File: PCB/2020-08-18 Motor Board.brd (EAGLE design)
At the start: 66 x 88.9 mm, 21 parts

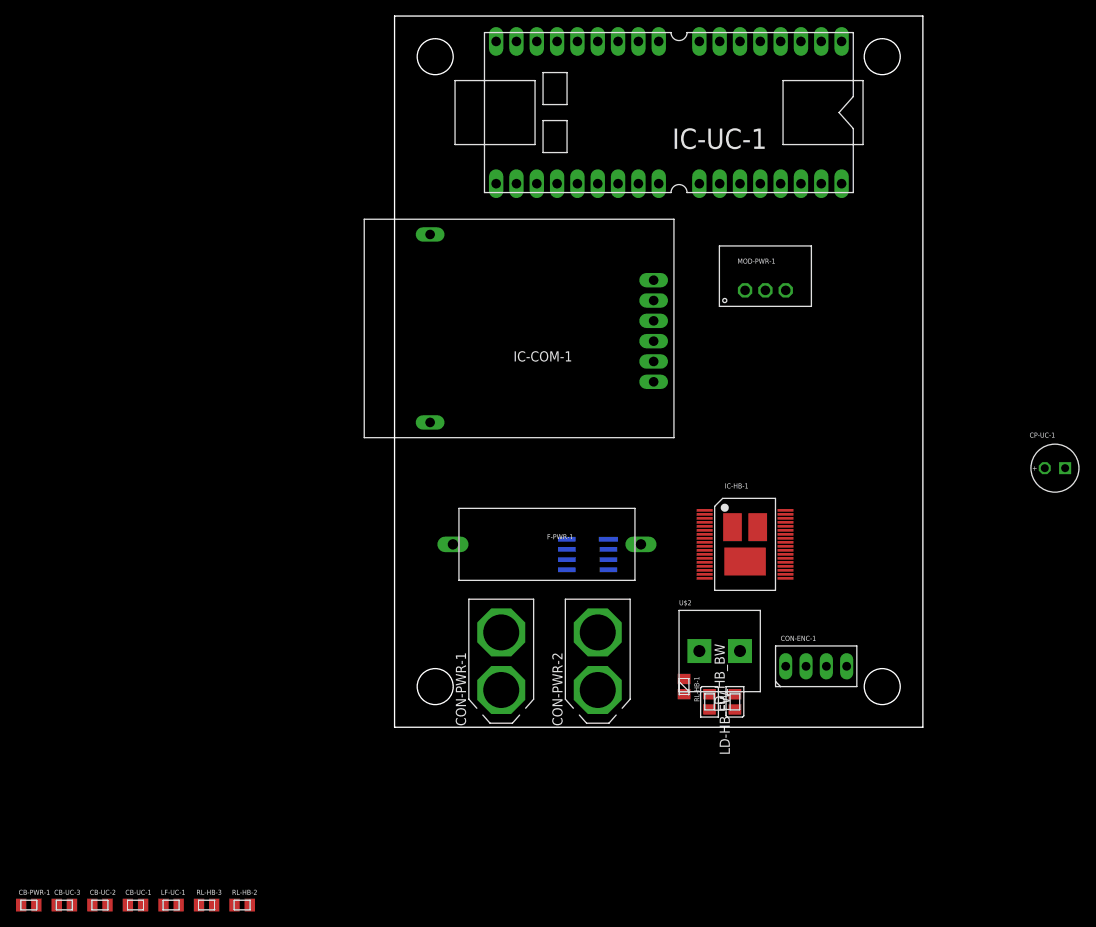
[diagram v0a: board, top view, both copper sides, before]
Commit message: updates schematics, dimensions and placement.
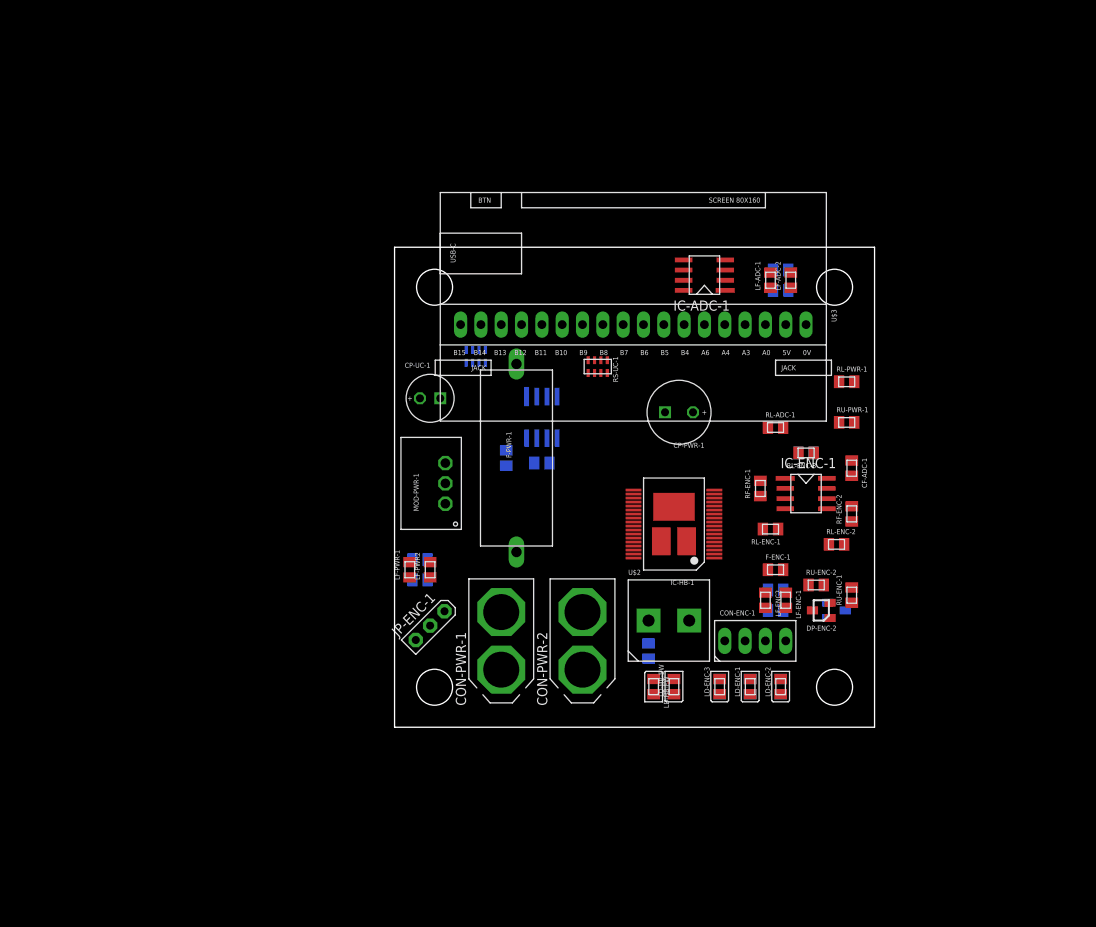
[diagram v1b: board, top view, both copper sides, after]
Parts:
- removed CB-PWR-1, CB-UC-1, CB-UC-2: 100n, Passives:SMD-M2012
- removed CB-UC-3: 10n, Passives:SMD-M2012
- removed IC-COM-1: MODULE-RS485-3MM5-JACK-X2, 2020-08-18 Motor Board:MODULE-RS485-3MM5-JACK-X2
- removed IC-UC-1: LONGAN-NANO, 2020-08-18 Motor Board:LONGAN-NANO
- removed LD_HB_BW: RED, Passives:SMD-M2012-POL
- removed LF-UC-1: BEAD 500mA, Passives:SMD-M2012
- removed RL-HB-2, RL-HB-3: 2.2K, Passives:SMD-M2012
- added CB-ADC-1, CB-ADC-2, CB-ENC-1, CB-ENC-2, CB-PWR-2, CB-PWR-3, CB-PWR1: 100n, Passives:SMD-M2012
- added CF-ADC-1, CF-PWR-1: 10n, Passives:SMD-M2012
- added CP-PWR-1: C+-TH3.5-8.0, Passives:TH-BARREL-3M5-8M0
- added DP-ENC-1, DP-ENC-2: BAT54S-SOT23, 2020-08-18 Motor Board:SOT23
- added F-ENC-1: 500mA, Passives:SMD-M2012
- added IC-ADC-1: MCP6282-SO8, 2020-08-18 Motor Board:SO8
- added IC-ENC-1: LM393-SO8, 2020-08-18 Motor Board:SO8
- added JP-ENC-1: (no value), 2020-08-18 Motor Board:1X03
- added LD-ENC-1, LD-ENC-2, LD-ENC-3: GREEN, Passives:SMD-M2012-POL
- added LD-HB-BW: RED, Passives:SMD-M2012-POL
- added LF-ADC-1, LF-ADC-2, LF-ENC-1, LF-ENC2, LF-PWR-1, LF-PWR2: BEAD 500mA, Passives:SMD-M2012
- added RF-ENC-1, RF-ENC-2, RL-ADC-1, RL-ENC-1, RL-ENC-2, RL-ENC-3, RL-PWR-1, RU-ENC-3, RU-PWR-1: 2.2K, Passives:SMD-M2012
- added RS-ENC-1, RS-ENC-2, RS-ENC-3, RU-ENC-1, RU-ENC-2: 330, Passives:SMD-M2012
- added RS-UC-1, RS-UC-2: RX4-M2012-X4, Passives:SMD-M2012-X4
- added U$3: MODULE-LONGAN-NANO, 2020-08-18 Motor Board:MODULE-LONGAN-NANO
- moved CP-UC-1 78.6 mm to (4.45, 41.1)
- moved MOD-PWR-1 46.7 mm to (6.35, 30.5), turned to 90 degrees
- moved IC-PWR-1 18.1 mm to (18.4, 38.7), turned to 180 degrees
- moved F-PWR-1 11.4 mm to (15.2, 33.7), turned to 90 degrees
- moved IC-HB-1 9.25 mm to (34.9, 25.4), turned to 90 degrees
- moved CON-ENC-1 8.25 mm to (45.1, 10.8)
- moved U$2 7.41 mm to (34.3, 13.3)
- moved LD-HB-FW 7.24 mm to (32.4, 5.08)
- moved RL-HB-1 6.29 mm to (31.8, 9.53), flipped to the bottom
- moved CON-PWR-2 3.17 mm to (23.5, 10.8)
- moved CON-PWR-1 2.54 mm to (13.3, 10.8)
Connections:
- removed net 3V3: IC-UC-1.19
- removed net N$10: IC-HB-1.20
- removed net N$17: CON-ENC-1.3
- removed net N$18: CON-ENC-1.4
- removed net N$6: IC-HB-1.16
- removed net N$7: IC-HB-1.21
- removed net N$8: IC-HB-1.15
- removed net UC-HB-INA-SEL0: IC-UC-1.31
- removed net VBAT: IC-UC-1.1
- new net ENC-BIAS: IC-ENC-1.2, IC-ENC-1.6, RL-ENC-3.1, RU-ENC-3.2
- new net ENC-CHA: CON-ENC-1.3, DP-ENC-1.3, RL-ENC-1.1, RU-ENC-1.1
- new net ENC-CHB: CON-ENC-1.4, DP-ENC-2.3, RL-ENC-2.1, RU-ENC-2.1
- new net HB-INA: IC-HB-1.16, RS-UC-1.2B
- new net HB-INB: IC-HB-1.21, RS-UC-1.4B
- new net HB-MSENSE-EN: IC-HB-1.20, RS-UC-2.2B
- new net HB-PWM: IC-HB-1.17, RS-UC-1.1B
- new net HB-SEL0: IC-HB-1.15, RS-UC-1.3B
- new net HB-SEL1: IC-HB-1.22, RS-UC-2.1B
- new net HB-SENSE: IC-ADC-1.3, IC-HB-1.19, RL-ADC-1.1
- new net N$12: LD-ENC-1.-, RS-ENC-1.1
- new net N$13: CB-PWR-2.2, LF-PWR-1.2, MOD-PWR-1.VIN
- new net N$14: CB-ENC-1.2, F-ENC-1.2, LF-ENC-1.1
- new net N$15: LD-ENC-3.-, RS-ENC-3.1
- new net N$16: RS-UC-2.4A
- new net N$19: RS-UC-2.3B
- new net N$4: IC-ENC-1.3, RF-ENC-1.1, RL-ENC-1.2
- new net PWR-SENSE-VIN: CF-ADC-1.1, IC-ADC-1.5, RL-PWR-1.1, RU-PWR-1.2
- new net UC-HB-INA: RS-UC-1.2A, U$3.B8
- new net UC-HB-SEL0: RS-UC-1.3A, U$3.B7
- new net UC-PWR-SENSE-IIN: IC-PWR-1.7, U$3.A6
- new net VENC#+: F-ENC-1.1, JP-ENC-1.2
- net MOT+: now also IC-HB-1.11, IC-HB-1.12, IC-HB-1.13, IC-HB-1.14, IC-HB-1.2, IC-HB-1.8, IC-HB-1.9, IC-HB-1.PAD2, LD-HB-BW.-; no longer IC-HB-1.23, IC-HB-1.24, IC-HB-1.25, IC-HB-1.26, IC-HB-1.28, IC-HB-1.29, IC-HB-1.35, IC-HB-1.PAD3, LD_HB_BW.-
- net MOT-: now also IC-HB-1.23, IC-HB-1.24, IC-HB-1.25, IC-HB-1.26, IC-HB-1.28, IC-HB-1.29, IC-HB-1.35, IC-HB-1.PAD3; no longer IC-HB-1.11, IC-HB-1.12, IC-HB-1.13, IC-HB-1.14, IC-HB-1.2, IC-HB-1.8, IC-HB-1.9, IC-HB-1.PAD2
- net N$1: now also LD-HB-BW.+; no longer LD_HB_BW.+
- net N$11: now also IC-ENC-1.5, RF-ENC-2.1, RL-ENC-2.2; no longer IC-HB-1.19
- net N$2: now also CF-PWR-1.2; no longer CB-UC-3.2
- net N$20: now also RS-UC-2.4B; no longer IC-PWR-1.7
- net N$5: now also LD-ENC-2.-, RS-ENC-2.1; no longer IC-HB-1.17
- net N$9: now also RS-UC-2.3A; no longer IC-HB-1.22
- net UC-COM-RXE#: now also U$3.B13; no longer IC-COM-1.RXEN#, IC-UC-1.21
- net UC-COM-RXI: now also U$3.B11; no longer IC-COM-1.RXO, IC-UC-1.16
- net UC-COM-TXE: now also U$3.B12; no longer IC-COM-1.TXEN, IC-UC-1.20
- net UC-COM-TXO: now also U$3.B10; no longer IC-COM-1.TXI, IC-UC-1.15
- net UC-ENC-CHA: now also IC-ENC-1.1, LD-ENC-1.+, RF-ENC-1.2, U$3.B4; no longer IC-UC-1.27
- net UC-ENC-CHB: now also IC-ENC-1.7, LD-ENC-2.+, RF-ENC-2.2, U$3.B5; no longer IC-UC-1.28
- net UC-HB-INB: now also RS-UC-1.4A, U$3.B9; no longer IC-UC-1.32
- net UC-HB-MSENSE-EN: now also RS-UC-2.2A, U$3.B15; no longer IC-UC-1.8
- net UC-HB-PWM: now also RS-UC-1.1A, U$3.B6; no longer IC-UC-1.29
- net UC-HB-SEL1: now also RS-UC-2.1A, U$3.B14; no longer IC-UC-1.30
- net UC-HB-SENSE-IOUT: now also IC-ADC-1.1, IC-ADC-1.2, U$3.A0; no longer IC-UC-1.5
- net UC-PWR-SENSE-VIN: now also IC-ADC-1.6, IC-ADC-1.7, U$3.A4; no longer IC-UC-1.9, RL-HB-2.2, RL-HB-3.1
- net VADC+: now also CB-ADC-2.2, CB-PWR-3.1, CF-PWR-1.1, IC-ADC-1.8, LF-ADC-1.2; no longer CB-PWR-1.1, CB-UC-2.2, LF-UC-1.2
- net VADC-: now also CB-ADC-2.1, CB-PWR-3.2, IC-ADC-1.4, IC-PWR-1.5, LF-ADC-2.2, RL-ADC-1.2; no longer CB-UC-1.1, CB-UC-2.1
- net VENC+: now also CB-ENC-2.2, DP-ENC-1.2, DP-ENC-2.2, IC-ENC-1.8, LD-ENC-3.+, LF-ENC-1.2, RU-ENC-1.2, RU-ENC-2.2, RU-ENC-3.1
- net VENC-: now also CB-ENC-2.1, DP-ENC-1.1, DP-ENC-2.1, IC-ENC-1.4, LF-ENC2.2, RL-ENC-3.2
- net VIN#+: now also CB-PWR1.2, CP-PWR-1.+, LF-PWR-1.1, RU-PWR-1.1; no longer MOD-PWR-1.VIN, RL-HB-2.1
- net VIN+: now also JP-ENC-1.1
- net VIN-: now also CB-PWR1.1, CP-PWR-1.-, LF-PWR2.1; no longer MOD-PWR-1.COM
- net VUC+: now also CB-ADC-1.2, CP-UC-1.+, JP-ENC-1.3, LF-ADC-1.1, U$3.5V; no longer CB-UC-1.2, IC-COM-1.5V0, IC-UC-1.18, LF-UC-1.1
- net VUC-: now also CB-ADC-1.1, CB-ENC-1.1, CB-PWR-2.1, CF-ADC-1.2, CP-UC-1.-, LF-ADC-2.1, LF-ENC2.1, LF-PWR2.2, MOD-PWR-1.COM, RL-PWR-1.2, RS-ENC-1.2, RS-ENC-2.2, RS-ENC-3.2, U$3.0V; no longer CB-PWR-1.2, CB-UC-3.1, IC-COM-1.0V0, IC-PWR-1.5, IC-UC-1.33, IC-UC-1.34, RL-HB-3.2
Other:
- board size 66 x 88.9 mm -> 60 x 60 mm
